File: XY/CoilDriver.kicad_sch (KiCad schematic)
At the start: 27 parts, among them Q1 IRLML2803, Q2 SIRA99DP-T1-GE3, U2 DRV8235RTER

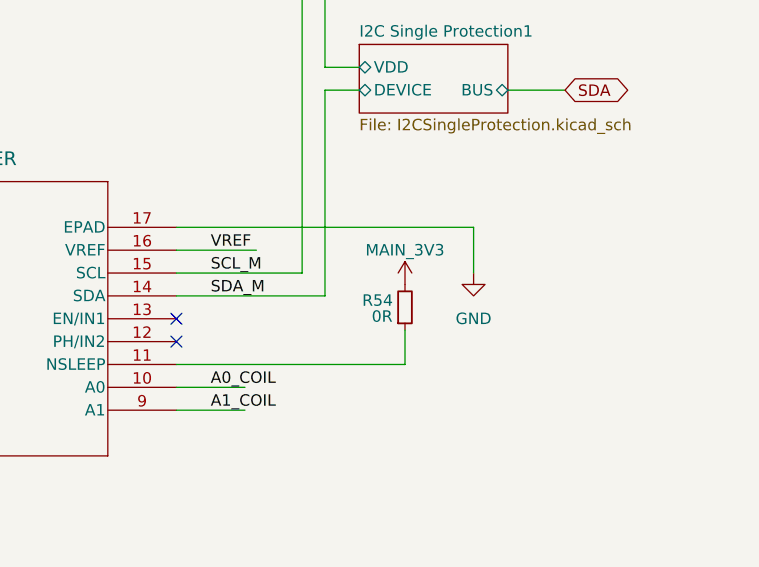
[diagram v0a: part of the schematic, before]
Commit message: Updated layout
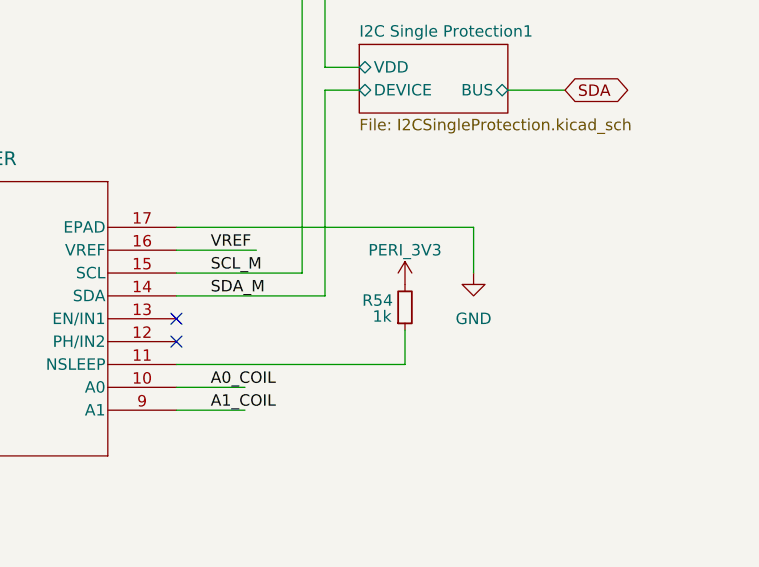
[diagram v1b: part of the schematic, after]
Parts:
- C26: footprint Capacitor_SMD:C_1206_3216Metric -> Capacitor_SMD:C_1210_3225Metric
- F2: footprint (none) -> Fuse:Fuse_0603_1608Metric
- R54: value 0R -> 1k
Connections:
- net MAIN_3V3: no longer R54.2
- new net PERI_3V3: R54.2
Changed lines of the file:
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@@
 			)
 		)
-		(property "Footprint" ""
+		(property "Footprint" "Fuse:Fuse_0603_1608Metric"
 			(at 78.74 31.75 0)
 			(effects
@@
 			)
 		)
-		(property "Value" "0R"
+		(property "Value" "1k"
 			(at 241.3 81.026 0)
 			(effects
@@
 			)
 		)
-		(property "Value" "MAIN_3V3"
+		(property "Value" "PERI_3V3"
 			(at 243.84 73.66 0)
 			(effects
@@
 			)
 		)
-		(property "Footprint" "Capacitor_SMD:C_1206_3216Metric"
+		(property "Footprint" "Capacitor_SMD:C_1210_3225Metric"
 			(at 134.9248 90.17 0)
 			(effects

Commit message: almost done
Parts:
- U2: symbol SolarPanels:DRV8235RTER -> Argus-IC:DRV8235RTER
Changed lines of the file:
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@@
 	)
 	(symbol
-		(lib_id "SolarPanels:DRV8235RTER")
+		(lib_id "Argus-IC:DRV8235RTER")
 		(at 167.64 71.12 0)
 		(unit 1)

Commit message: Uncommitted schematic changes
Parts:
- U2: footprint WQFN16_RTE_TEX -> Argus-IC:WQFN16_RTE_TEX
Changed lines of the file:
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@@
 			)
 		)
-		(property "Footprint" "WQFN16_RTE_TEX"
+		(property "Footprint" "Argus-IC:WQFN16_RTE_TEX"
 			(at 167.64 71.12 0)
 			(effects

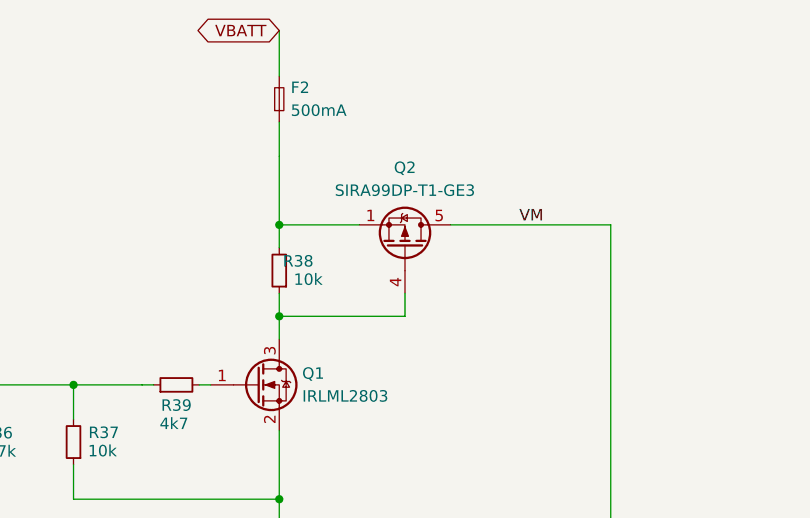
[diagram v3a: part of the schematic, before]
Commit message: Updated 3d models, footprints
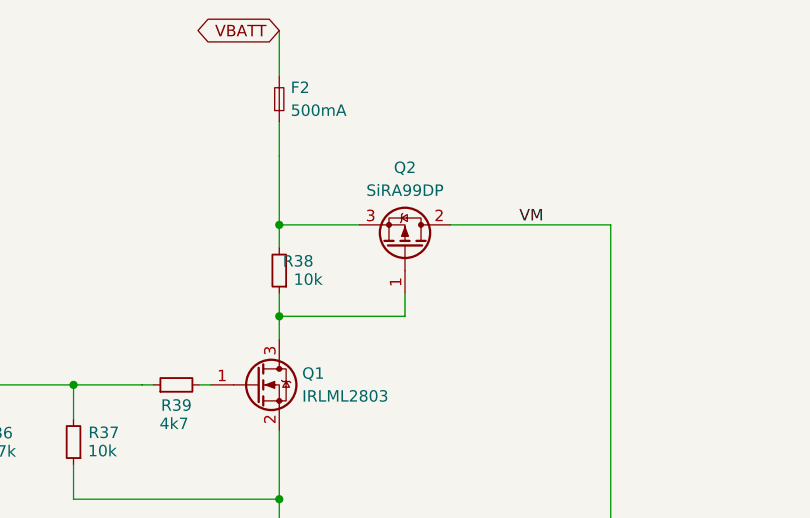
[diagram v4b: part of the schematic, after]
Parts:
- removed Q2: SIRA99DP-T1-GE3, Package_SO:PowerPAK_SO-8_Single, symbol Transistor_FET:Si7141DP
- added Q2: SiRA99DP, Argus-Miscellaneous:PowerPAK SO-8, symbol Argus-IC:Q_PMOS_GDS
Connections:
- net VM: now also Q2.2 (D)
- net at Q1.3 (D), R38.1: now also Q2.1 (G)
- net at F2.1, R38.2: now also Q2.3 (S)
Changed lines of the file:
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@@
+	)
+	(symbol
+		(lib_id "Argus-IC:Q_PMOS_GDS")
+		(at 92.71 48.26 270)
+		(mirror x)
+		(unit 1)
+		(exclude_from_sim no)
+		(in_bom yes)
+		(on_board yes)
+		(dnp no)
+		(property "Reference" "Q2"
+			(at 92.71 39.37 90)
+			(effects
+				(font
+					(size 1.27 1.27)
+				)
+			)
+		)
+		(property "Value" "SiRA99DP"
+			(at 92.71 41.91 90)
+			(effects
+				(font
+					(size 1.27 1.27)
+				)
+			)
+		)
+		(property "Footprint" "Argus-Miscellaneous:PowerPAK SO-8"
+			(at 95.25 43.18 0)
+			(effects
+				(font
+					(size 1.27 1.27)
+				)
+				(hide yes)
+			)
+		)
+		(property "Datasheet" "~"
+			(at 92.71 48.26 0)
+			(effects
+				(font
+					(size 1.27 1.27)
+				)
+				(hide yes)
+			)
+		)
+		(property "Description" "P-MOSFET transistor, gate/drain/source"
+			(at 92.71 48.26 0)
+			(effects
+				(font
+					(size 1.27 1.27)
+				)
+				(hide yes)
+			)
+		)
+		(pin "3"
+		)
+		(pin "2"
+		)
+		(pin "1"
+		)
+		(instances
+			(project "Avionics-SolarPanels"
+				(path "/92e58b76-9357-4452-b231-18fffdf58e73/757bbe31-359d-4282-a8be-b82658fcdbcd"
+					(reference "Q2")
+					(unit 1)
+				)
+			)
+		)
 	)
 	(symbol
@@
 					(unit 1)
 				)
-			)
-		)
-	)
-	(symbol
-		(lib_id "Transistor_FET:Si7141DP")
-		(at 92.71 48.26 270)
-		(mirror x)
-		(unit 1)
-		(exclude_from_sim no)
-		(in_bom yes)
-		(on_board yes)
-		(dnp no)
-		(property "Reference" "Q2"
-			(at 92.71 39.37 90)
-			(effects
-				(font
-					(size 1.27 1.27)
-				)
-			)
-		)
-		(property "Value" "SIRA99DP-T1-GE3"
-			(at 92.71 41.91 90)
-			(effects
-				(font
-					(size 1.27 1.27)
-				)
-			)
-		)
-		(property "Footprint" "Package_SO:PowerPAK_SO-8_Single"
-			(at 90.805 43.18 0)
-			(effects
-				(font
-					(size 1.27 1.27)
-					(italic yes)
-				)
-				(justify left)
-				(hide yes)
-			)
-		)
-		(property "Datasheet" "https://www.vishay.com/docs/65596/si7141dp.pdf"
-			(at 88.9 43.18 0)
-			(effects
-				(font
-					(size 1.27 1.27)
-				)
-				(justify left)
-				(hide yes)
-			)
-		)
-		(property "Description" "-60A Id, -20V Vds, 1.9 mOhm Ron, PowerPAK-8"
-			(at 92.71 48.26 0)
-			(effects
-				(font
-					(size 1.27 1.27)
-				)
-				(hide yes)
-			)
-		)
-		(pin "5"
-		)
-		(pin "2"
-		)
-		(pin "3"
-		)
-		(pin "4"
-		)
-		(pin "1"
-		)
-		(instances
-			(project "Avionics-SolarPanels"
-				(path "/92e58b76-9357-4452-b231-18fffdf58e73/757bbe31-359d-4282-a8be-b82658fcdbcd"
-					(reference "Q2")
-					(unit 1)
-				)
